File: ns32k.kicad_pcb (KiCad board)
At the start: 4 copper layers, 145.5 x 89.6 mm, 138 parts, among them J1 +5V SUPPLY, J2 3V3 Serial, J3 USB_C_USB2.0_16P, J4 RJ45, SW1 RESET, SW2 SW_DIP_x04, U1 NS32201, U10 74AHC373, U11 74AHC373, U12 74AHC138, U13 AS6C6416-55, U14 MT29F8G08ABACA, U15 MX29LV040C, U16 MX29LV040C, U17 ST16C550, U18 CP2102N, U19 74AHC32, U2 LM3671, U20 74AHC1GU04, U21 KSZ8851-16MLL, U22 74AHC245, U23 74AHC1GU04, U24 74AHC1GU04, U3 NS32016, U4 NS32082, U5 NS32202, U6 74AHC08, U7 74AHC245, U8 74AHC245, U9 74AHC373, Y1 12.00000MHz, Y2 7.3728MHz, Y3 25MHz

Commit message: various changes, add LCSC part #s
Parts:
- C11: value 22µF 25V X5R -> 22µF 25V
- C40, C41: value 10µF -> 10µF 16V
- D10, D11: value 1N4148 -> 1N4148 etc
- FB1, FB2, FB3: value MMZ1005D330C -> 330 @ 100
- L1: value 2.2µH -> 2.2uH 70MHz+ 1A+ 0.5Ω-
- R32, R33, R34, R35: value 49.9 1/2W -> 49.9 1/4W+
- SW2: value SW_DIP_x04 -> SW_DIP_x04 300w/50p mil
- U2: value LM3671 -> LM3671 3.3V
- moved R36 0.96 mm to (197.8, 71.1), turned to 90 degrees
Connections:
- net /PAV renamed /PAV33
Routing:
- net /Ethernet/~{INT_ETH}: track 115.3 -> 121.1 mm, vias 4 -> 2
- net Net-(U21A-~{P1LED0}): track 16.9 -> 21.6 mm, vias 2 -> 0
- net +3V3: track 101.0 -> 100.2 mm
- net /~{ETH}: track 68.4 -> 67.7 mm
- net GND: track 142.6 -> 141.9 mm

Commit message: revert crystal footprints back from LCSC parts
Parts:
- Y1: footprint Crystal:Crystal_SMD_3225-4Pin_3.2x2.5mm -> FH12000001:FH12000001
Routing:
- net GND: track 141.9 -> 141.5 mm, vias 114 -> 115
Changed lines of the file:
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@@
 		)
 	)
-	(footprint "Crystal:Crystal_SMD_3225-4Pin_3.2x2.5mm"
+	(footprint "FH12000001:FH12000001"
 		(layer "F.Cu")
 		(at 62.0522 131.5466 90)
-		(descr "SMD Crystal SERIES SMD3225/4 http://www.txccrystal.com/images/pdf/7m-accuracy.pdf, 3.2x2.5mm^2 package")
-		(tags "SMD SMT crystal")
 		(property "Reference" "Y1"
-			(at 0 -2.45 90)
+			(at 0.381 -2.286 90)
 			(layer "F.SilkS")
 			(effects
@@
 		)
 		(property "Value" "12.00000MHz"
-			(at 0 2.45 90)
+			(at 0.127 0 90)
 			(layer "F.Fab")
 			(effects
@@
 			)
 		)
-		(property "Footprint" "Crystal:Crystal_SMD_3225-4Pin_3.2x2.5mm"
+		(property "Footprint" "FH12000001:FH12000001"
 			(at 0 0 90)
-			(unlocked yes)
 			(layer "F.Fab")
 			(hide yes)
@@
 		(property "Datasheet" ""
 			(at 0 0 90)
-			(unlocked yes)
 			(layer "F.Fab")
 			(hide yes)
@@
 		(property "Description" ""
 			(at 0 0 90)
-			(unlocked yes)
 			(layer "F.Fab")
 			(hide yes)
@@
 		(sheetname "Power, Reset, OSC")
 		(sheetfile "power.kicad_sch")
-		(attr smd)
-		(fp_line
-			(start -2 -1.65)
-			(end -2 1.65)
-			(stroke
-				(width 0.12)
-				(type solid)
-			)
-			(layer "F.SilkS")
-		)
+		(attr through_hole)
 		(fp_line
-			(start -2 1.65)
-			(end 2 1.65)
+			(start -1.778 0.381)
+			(end -1.778 1.143)
 			(stroke
-				(width 0.12)
+				(width 0.15)
 				(type solid)
 			)
@@
 		)
 		(fp_line
-			(start 2.1 -1.7)
-			(end -2.1 -1.7)
-			(stroke
-				(width 0.05)
-				(type solid)
-			)
-			(layer "F.CrtYd")
-		)
-		(fp_line
-			(start -2.1 -1.7)
-			(end -2.1 1.7)
-			(stroke
-				(width 0.05)
-				(type solid)
-			)
-			(layer "F.CrtYd")
-		)
-		(fp_line
-			(start 2.1 1.7)
-			(end 2.1 -1.7)
-			(stroke
-				(width 0.05)
-				(type solid)
-			)
-			(layer "F.CrtYd")
-		)
-		(fp_line
-			(start -2.1 1.7)
-			(end 2.1 1.7)
-			(stroke
-				(width 0.05)
-				(type solid)
-			)
-			(layer "F.CrtYd")
-		)
-		(fp_line
-			(start 1.6 -1.25)
-			(end -1.6 -1.25)
-			(stroke
-				(width 0.1)
-				(type solid)
-			)
-			(layer "F.Fab")
-		)
-		(fp_line
-			(start -1.6 -1.25)
-			(end -1.6 1.25)
+			(start 1.524 -1.397)
+			(end 1.524 1.397)
 			(stroke
 				(width 0.1)
 				(type solid)
 			)
-			(layer "F.Fab")
+			(layer "F.CrtYd")
 		)
 		(fp_line
-			(start -1.6 0.25)
-			(end -0.6 1.25)
+			(start -1.524 -1.397)
+			(end 1.524 -1.397)
 			(stroke
 				(width 0.1)
 				(type solid)
 			)
-			(layer "F.Fab")
+			(layer "F.CrtYd")
 		)
 		(fp_line
-			(start 1.6 1.25)
-			(end 1.6 -1.25)
+			(start 1.524 1.397)
+			(end -1.524 1.397)
 			(stroke
 				(width 0.1)
 				(type solid)
 			)
-			(layer "F.Fab")
+			(layer "F.CrtYd")
 		)
 		(fp_line
-			(start -1.6 1.25)
-			(end 1.6 1.25)
+			(start -1.524 1.397)
+			(end -1.524 -1.397)
 			(stroke
 				(width 0.1)
 				(type solid)
 			)
-			(layer "F.Fab")
-		)
-		(fp_text user "${REFERENCE}"
-			(at 0 0 90)
-			(layer "F.Fab")
-			(effects
-				(font
-					(size 0.7 0.7)
-					(thickness 0.105)
-				)
-			)
+			(layer "F.CrtYd")
 		)
 		(pad "1" smd rect
-			(at -1.1 0.85 90)
-			(size 1.4 1.2)
+			(at -0.925 0.775 90)
+			(size 1 0.95)
 			(layers "F.Cu" "F.Paste" "F.Mask")
 			(net 115 "Net-(C1-Pad1)")
@@
 			(pintype "passive")
 		)
-		(pad "2" smd rect
-			(at 1.1 0.85 90)
-			(size 1.4 1.2)
+		(pad "2" smd roundrect
+			(at 0.925 0.775 90)
+			(size 1 0.95)
 			(layers "F.Cu" "F.Paste" "F.Mask")
+			(roundrect_rratio 0.25)
 			(net 1 "GND")
 			(pinfunction "2")
 			(pintype "passive")
 		)
-		(pad "3" smd rect
-			(at 1.1 -0.85 90)
-			(size 1.4 1.2)
+		(pad "3" smd roundrect
+			(at 0.925 -0.775 90)
+			(size 1 0.95)
 			(layers "F.Cu" "F.Paste" "F.Mask")
+			(roundrect_rratio 0.25)
 			(net 23 "Net-(U1B-XIN)")
 			(pinfunction "3")
 			(pintype "passive")
 		)
-		(pad "4" smd rect
-			(at -1.1 -0.85 90)
-			(size 1.4 1.2)
+		(pad "4" smd roundrect
+			(at -0.925 -0.775 90)
+			(size 1 0.95)
 			(layers "F.Cu" "F.Paste" "F.Mask")
+			(roundrect_rratio 0.25)
 			(net 1 "GND")
 			(pinfunction "4")
 			(pintype "passive")
 		)
-		(model "${KICAD8_3DMODEL_DIR}/Crystal.3dshapes/Crystal_SMD_3225-4Pin_3.2x2.5mm.wrl"
-			(offset
-				(xyz 0 0 0)
-			)
-			(scale
-				(xyz 1 1 1)
-			)
-			(rotate
-				(xyz 0 0 0)
-			)
-		)
 	)
 	(footprint "Resistor_SMD:R_0402_1005Metric"
@@
 	)
 	(segment
+		(start 170.5102 89.5096)
+		(end 170.3578 89.5096)
+		(width 0.2032)
+		(layer "F.Cu")
+		(net 1)
+	)
+	(segment
 		(start 166.553 133.1836)
 		(end 166.553 134.5148)
@@
 	)
 	(segment
-		(start 171.0208 89.143827)
-		(end 171.3142 88.850427)
-		(width 0.2032)
-		(layer "F.Cu")
-		(net 1)
-	)
-	(segment
 		(start 171.859 112.1576)
 		(end 172.708944 111.307656)
@@
 	)
 	(segment
-		(start 171.0208 90.0202)
-		(end 171.0208 89.143827)
-		(width 0.2032)
-		(layer "F.Cu")
-		(net 1)
-	)
-	(segment
 		(start 146.13 134.743198)
 		(end 145.999198 134.874)
@@
 	)
 	(segment
+		(start 171.0208 90.0202)
+		(end 170.5102 89.5096)
+		(width 0.2032)
+		(layer "F.Cu")
+		(net 1)
+	)
+	(segment
 		(start 170.114 104.8711)
 		(end 170.114 106.1822)
@@
 	)
 	(via
-		(at 171.323 86.2584)
+		(at 171.2976 85.1154)
 		(size 0.6)
 		(drill 0.3)
@@
 	)
 	(via
-		(at 171.3142 88.850427)
+		(at 170.3578 89.5096)
 		(size 0.6)
 		(drill 0.3)
@@
 		(net 1)
 	)
+	(via
+		(at 171.6278 87.2998)
+		(size 0.6)
+		(drill 0.3)
+		(layers "F.Cu" "B.Cu")
+		(free yes)
+		(net 1)
+	)

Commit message: restore L1 TY NHR24xx FP
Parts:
- L1: value 2.2uH 70MHz+ 1A+ 0.5Ω- -> 2.2µH 70MHz+ 1A+ 0.5Ω-; footprint Inductor_SMD:L_0805_2012Metric -> Inductor_SMD:L_Taiyo-Yuden_NR-24xx
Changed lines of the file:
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@@
 		)
 	)
-	(footprint "Inductor_SMD:L_0805_2012Metric"
+	(footprint "Inductor_SMD:L_Taiyo-Yuden_NR-24xx"
 		(layer "F.Cu")
 		(at 105.791 123.3336 -90)
-		(descr "Inductor SMD 0805 (2012 Metric), square (rectangular) end terminal, IPC_7351 nominal, (Body size source: IPC-SM-782 page 80, https://www.pcb-3d.com/wordpress/wp-content/uploads/ipc-sm-782a_amendment_1_and_2.pdf), generated with kicad-footprint-generator")
-		(tags "inductor")
+		(descr "Inductor, Taiyo Yuden, NR series, Taiyo-Yuden_NR-24xx, 2.4mmx2.4mm")
+		(tags "inductor taiyo-yuden nr smd")
 		(property "Reference" "L1"
-			(at 0 -1.55 -90)
+			(at 0 -2.2 -90)
 			(layer "F.SilkS")
 			(effects
@@
 			)
 		)
-		(property "Value" "2.2uH 70MHz+ 1A+ 0.5Ω-"
-			(at 0 1.55 -90)
+		(property "Value" "2.2µH 70MHz+ 1A+ 0.5Ω-"
+			(at 0 2.7 -90)
 			(layer "F.Fab")
 			(effects
@@
 			)
 		)
-		(property "Footprint" "Inductor_SMD:L_0805_2012Metric"
+		(property "Footprint" "Inductor_SMD:L_Taiyo-Yuden_NR-24xx"
 			(at 0 0 -90)
 			(unlocked yes)
@@
 		(attr smd)
 		(fp_line
-			(start -0.399622 0.56)
-			(end 0.399622 0.56)
+			(start -1.2 1.3)
+			(end 1.2 1.3)
 			(stroke
 				(width 0.12)
@@
 		)
 		(fp_line
-			(start -0.399622 -0.56)
-			(end 0.399622 -0.56)
+			(start -1.2 -1.3)
+			(end 1.2 -1.3)
 			(stroke
 				(width 0.12)
@@
 		)
 		(fp_line
-			(start -1.75 0.85)
-			(end -1.75 -0.85)
+			(start -1.5 1.5)
+			(end 1.5 1.5)
 			(stroke
 				(width 0.05)
@@
 		)
 		(fp_line
-			(start 1.75 0.85)
-			(end -1.75 0.85)
+			(start 1.5 1.5)
+			(end 1.5 -1.5)
 			(stroke
 				(width 0.05)
@@
 		)
 		(fp_line
-			(start -1.75 -0.85)
-			(end 1.75 -0.85)
+			(start -1.5 -1.5)
+			(end -1.5 1.5)
 			(stroke
 				(width 0.05)
@@
 		)
 		(fp_line
-			(start 1.75 -0.85)
-			(end 1.75 0.85)
+			(start 1.5 -1.5)
+			(end -1.5 -1.5)
 			(stroke
 				(width 0.05)
@@
 		)
 		(fp_line
-			(start -1 0.45)
-			(end -1 -0.45)
+			(start -0.725 1.2)
+			(end 0.725 1.2)
 			(stroke
 				(width 0.1)
@@
 		)
 		(fp_line
-			(start 1 0.45)
-			(end -1 0.45)
+			(start -1.2 0.725)
+			(end -0.725 1.2)
 			(stroke
 				(width 0.1)
@@
 		)
 		(fp_line
-			(start -1 -0.45)
-			(end 1 -0.45)
+			(start 1.2 0.725)
+			(end 0.725 1.2)
 			(stroke
 				(width 0.1)
@@
 		)
 		(fp_line
-			(start 1 -0.45)
-			(end 1 0.45)
+			(start -1.2 -0.725)
+			(end -1.2 0.725)
+			(stroke
+				(width 0.1)
+				(type solid)
+			)
+			(layer "F.Fab")
+		)
+		(fp_line
+			(start -1.2 -0.725)
+			(end -0.725 -1.2)
+			(stroke
+				(width 0.1)
+				(type solid)
+			)
+			(layer "F.Fab")
+		)
+		(fp_line
+			(start 1.2 -0.725)
+			(end 1.2 0.725)
+			(stroke
+				(width 0.1)
+				(type solid)
+			)
+			(layer "F.Fab")
+		)
+		(fp_line
+			(start 1.2 -0.725)
+			(end 0.725 -1.2)
+			(stroke
+				(width 0.1)
+				(type solid)
+			)
+			(layer "F.Fab")
+		)
+		(fp_line
+			(start -0.725 -1.2)
+			(end 0.725 -1.2)
 			(stroke
 				(width 0.1)
@@
 				(font
 					(size 0.5 0.5)
-					(thickness 0.08)
+					(thickness 0.075)
 				)
 			)
 		)
-		(pad "1" smd roundrect
-			(at -1.0625 0 270)
-			(size 0.875 1.2)
+		(pad "1" smd rect
+			(at -0.725 0 270)
+			(size 0.7 2)
 			(layers "F.Cu" "F.Paste" "F.Mask")
-			(roundrect_rratio 0.25)
 			(net 130 "Net-(U2-SW)")
 			(pintype "passive")
 		)
-		(pad "2" smd roundrect
-			(at 1.0625 0 270)
-			(size 0.875 1.2)
+		(pad "2" smd rect
+			(at 0.725 0 270)
+			(size 0.7 2)
 			(layers "F.Cu" "F.Paste" "F.Mask")
-			(roundrect_rratio 0.25)
 			(net 2 "+3V3")
 			(pintype "passive")
 		)
-		(model "${KICAD8_3DMODEL_DIR}/Inductor_SMD.3dshapes/L_0805_2012Metric.wrl"
+		(model "${KICAD8_3DMODEL_DIR}/Inductor_SMD.3dshapes/L_Taiyo-Yuden_NR-24xx.wrl"
 			(offset
 				(xyz 0 0 0)
@@
 	)
 	(segment
-		(start 105.4855 122.5766)
-		(end 105.791 122.2711)
+		(start 105.759 122.5766)
+		(end 105.791 122.6086)
 		(width 0.4064)
 		(layer "F.Cu")
@@
 	(segment
 		(start 103.1185 122.5766)
-		(end 105.4855 122.5766)
+		(end 105.759 122.5766)
 		(width 0.4064)
 		(layer "F.Cu")

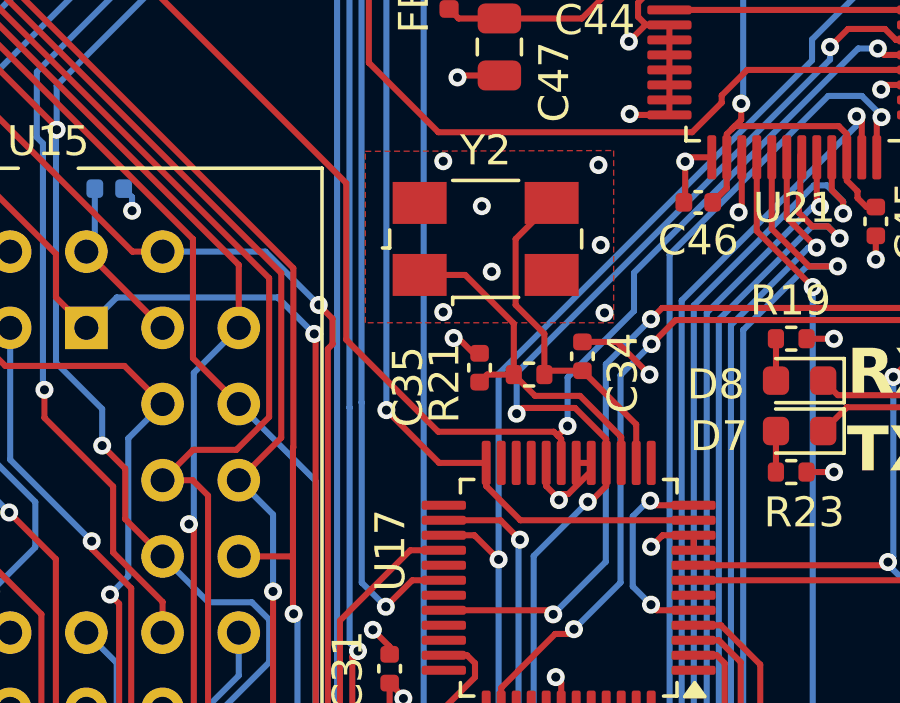
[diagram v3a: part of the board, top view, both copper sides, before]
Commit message: AS is active high, and we tie it to GND
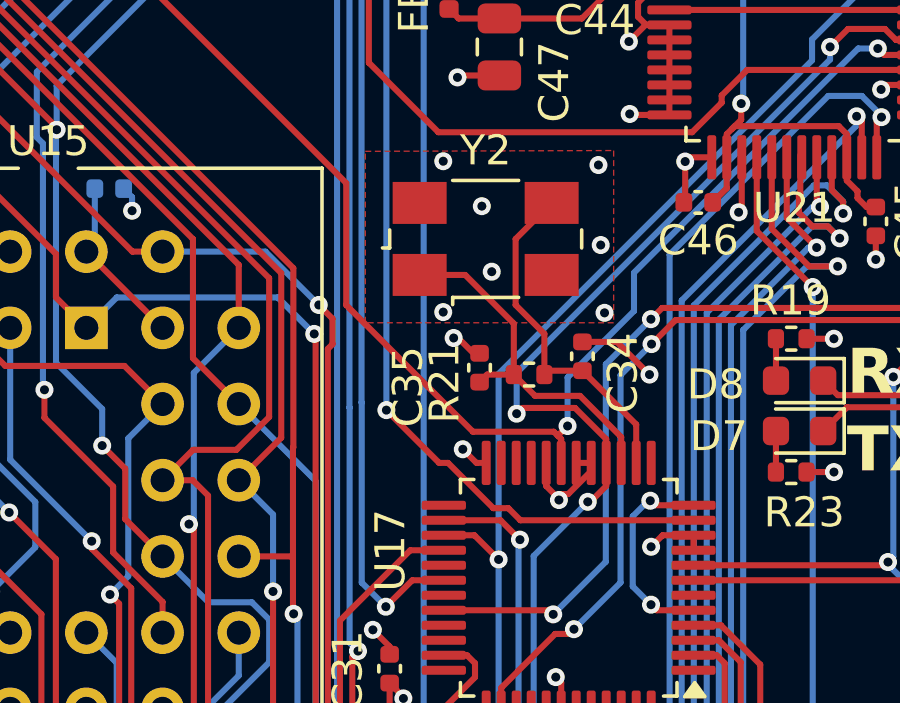
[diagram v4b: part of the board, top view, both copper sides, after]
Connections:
- U17 pad 24: /~{SER_CS} -> GND
- U5 pad 27: Net-(U3A-~{RST}/ABT) -> /Ethernet/~{RESET}
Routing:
- net GND: track 141.5 -> 142.5 mm, vias 115 -> 116
- net /~{RD33}: track 278.4 -> 277.7 mm
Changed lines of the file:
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@@
 			(layers "*.Cu" "*.Mask")
 			(remove_unused_layers no)
-			(net 8 "Net-(U3A-~{RST}{slash}ABT)")
+			(net 206 "/Ethernet/~{RESET}")
 			(pinfunction "~{RST}")
 			(pintype "input")
@@
 			(layers "F.Cu" "F.Paste" "F.Mask")
 			(roundrect_rratio 0.25)
-			(net 5 "/~{SER_CS}")
-			(pinfunction "~{AS}")
+			(net 1 "GND")
+			(pinfunction "AS")
 			(pintype "input")
 		)
@@
 	)
 	(segment
+		(start 171.1175 93.6729)
+		(end 170.6626 93.218)
+		(width 0.2)
+		(layer "F.Cu")
+		(net 1)
+	)
+	(segment
 		(start 130.937 71.7208)
 		(end 130.9624 71.6954)
@@
 	)
 	(segment
+		(start 171.4432 93.6729)
+		(end 171.1175 93.6729)
+		(width 0.2)
+		(layer "F.Cu")
+		(net 1)
+	)
+	(segment
 		(start 117.6225 54.1947)
 		(end 125.4252 54.1947)
@@
 	)
 	(via
+		(at 170.6626 93.218)
+		(size 0.6)
+		(drill 0.3)
+		(layers "F.Cu" "B.Cu")
+		(net 1)
+	)
+	(via
 		(at 178.053 134.534)
 		(size 0.6)
@@
 	(segment
 		(start 169.8741 93.6729)
+		(end 170.171028 93.6729)
+		(width 0.2032)
+		(layer "F.Cu")
+		(net 5)
+	)
+	(segment
+		(start 169.8741 93.6729)
 		(end 168.115 91.9138)
 		(width 0.2032)
@@
 	)
 	(segment
-		(start 171.4432 93.6729)
-		(end 169.8741 93.6729)
+		(start 170.171028 93.6729)
+		(end 171.680328 95.1822)
 		(width 0.2032)
 		(layer "F.Cu")
@@
 	)
 	(segment
+		(start 171.680328 95.1822)
+		(end 172.180328 95.1822)
+		(width 0.2032)
+		(layer "F.Cu")
+		(net 5)
+	)
+	(segment
 		(start 135.856001 56.7146)
 		(end 135.5544 57.016201)
@@
 	)
 	(segment
-		(start 172.583528 95.5854)
-		(end 171.4432 94.445072)
-		(width 0.2032)
-		(layer "F.Cu")
-		(net 5)
-	)
-	(segment
-		(start 171.4432 94.445072)
-		(end 171.4432 93.6729)
+		(start 172.180328 95.1822)
+		(end 172.583528 95.5854)
 		(width 0.2032)
 		(layer "F.Cu")
@@
 	)
 	(segment
+		(start 170.999902 92.6338)
+		(end 173.6956 92.6338)
+		(width 0.2032)
+		(layer "F.Cu")
+		(net 84)
+	)
+	(segment
+		(start 166.7764 84.3446)
+		(end 166.7764 88.410298)
+		(width 0.2032)
+		(layer "F.Cu")
+		(net 84)
+	)
+	(segment
 		(start 174.553 114.630772)
 		(end 174.553 113.7046)
@@
 	)
 	(segment
-		(start 173.6956 92.6338)
-		(end 173.8301 92.7683)
-		(width 0.2032)
-		(layer "F.Cu")
-		(net 84)
-	)
-	(segment
 		(start 158.641903 93.095894)
 		(end 159.4104 93.864391)
@@
 	)
 	(segment
+		(start 160.3248 77.893)
+		(end 166.7764 84.3446)
+		(width 0.2032)
+		(layer "F.Cu")
+		(net 84)
+	)
+	(segment
 		(start 151.3618 76.7246)
 		(end 145.60421 76.7246)
@@
 	)
 	(segment
-		(start 166.7764 84.3446)
-		(end 166.7764 89.56559)
+		(start 173.6956 92.6338)
+		(end 173.8301 92.7683)
 		(width 0.2032)
 		(layer "F.Cu")
@@
 	)
 	(segment
+		(start 166.7764 88.410298)
+		(end 170.999902 92.6338)
+		(width 0.2032)
+		(layer "F.Cu")
+		(net 84)
+	)
+	(segment
 		(start 163.2712 75.099)
 		(end 163.2712 72.8726)
@@
 	)
 	(segment
-		(start 166.7764 89.56559)
-		(end 169.84461 92.6338)
-		(width 0.2032)
-		(layer "F.Cu")
-		(net 84)
-	)
-	(segment
 		(start 145.60421 76.7246)
 		(end 143.102969 79.225841)
 		(width 0.2032)
 		(layer "F.Cu")
-		(net 84)
-	)
-	(segment
-		(start 169.84461 92.6338)
-		(end 173.6956 92.6338)
-		(width 0.2032)
-		(layer "F.Cu")
-		(net 84)
-	)
-	(segment
-		(start 160.3248 77.893)
-		(end 166.7764 84.3446)
-		(width 0.2032)
-		(layer "F.Cu")
